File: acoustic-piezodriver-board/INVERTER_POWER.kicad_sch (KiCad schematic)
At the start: 64 parts, among them Q501 AO3400A, Q502 AO3400A, U501 NCE6005AS, U502 LM3478MM, U503 NCE6005AS, U504 LM3478MM

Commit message: [schematic] added adc for temperature measurement, current sense resistors, [layout] component placement, connector placement
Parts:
- added C523, C524: 0.1uF, Capacitor_SMD:C_0402_1005Metric, symbol Device:C_Small
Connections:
- net +BATT: now also C523.1, C524.1
- net GND: now also C523.2, C524.2
- net VDC renamed VDC_P
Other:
- moved on the sheet: R511

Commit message: [piezodriver] Added resistive divider (next) come up with a solution for current sensing (galvanic isolation?)
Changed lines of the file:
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@@
 	(text "DC-DC (SEPIC) VBAT -> 10 V\nCapacitance datasheet recommendations\n- Input capacitance (10-20 uF)\n- Output capacitance (100 uF) "
 		(exclude_from_sim no)
-		(at 334.772 35.306 0)
+		(at 349.758 28.448 0)
 		(effects
 			(font

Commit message: found hal-sensor, replaced with different one for lower voltage signal source impedance, reorganised schematic
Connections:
- net VDC_P: no longer C516.1, C517.1, C518.1, C519.1, D504.1 (K), R512.1
- new net VINV_P: C516.1, C517.1, C518.1, C519.1, D504.1 (K), R512.1
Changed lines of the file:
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@@
 		)
 	)
-	(hierarchical_label "VDC_P"
+	(hierarchical_label "VINV_P"
 		(shape bidirectional)
 		(at 379.73 185.42 0)

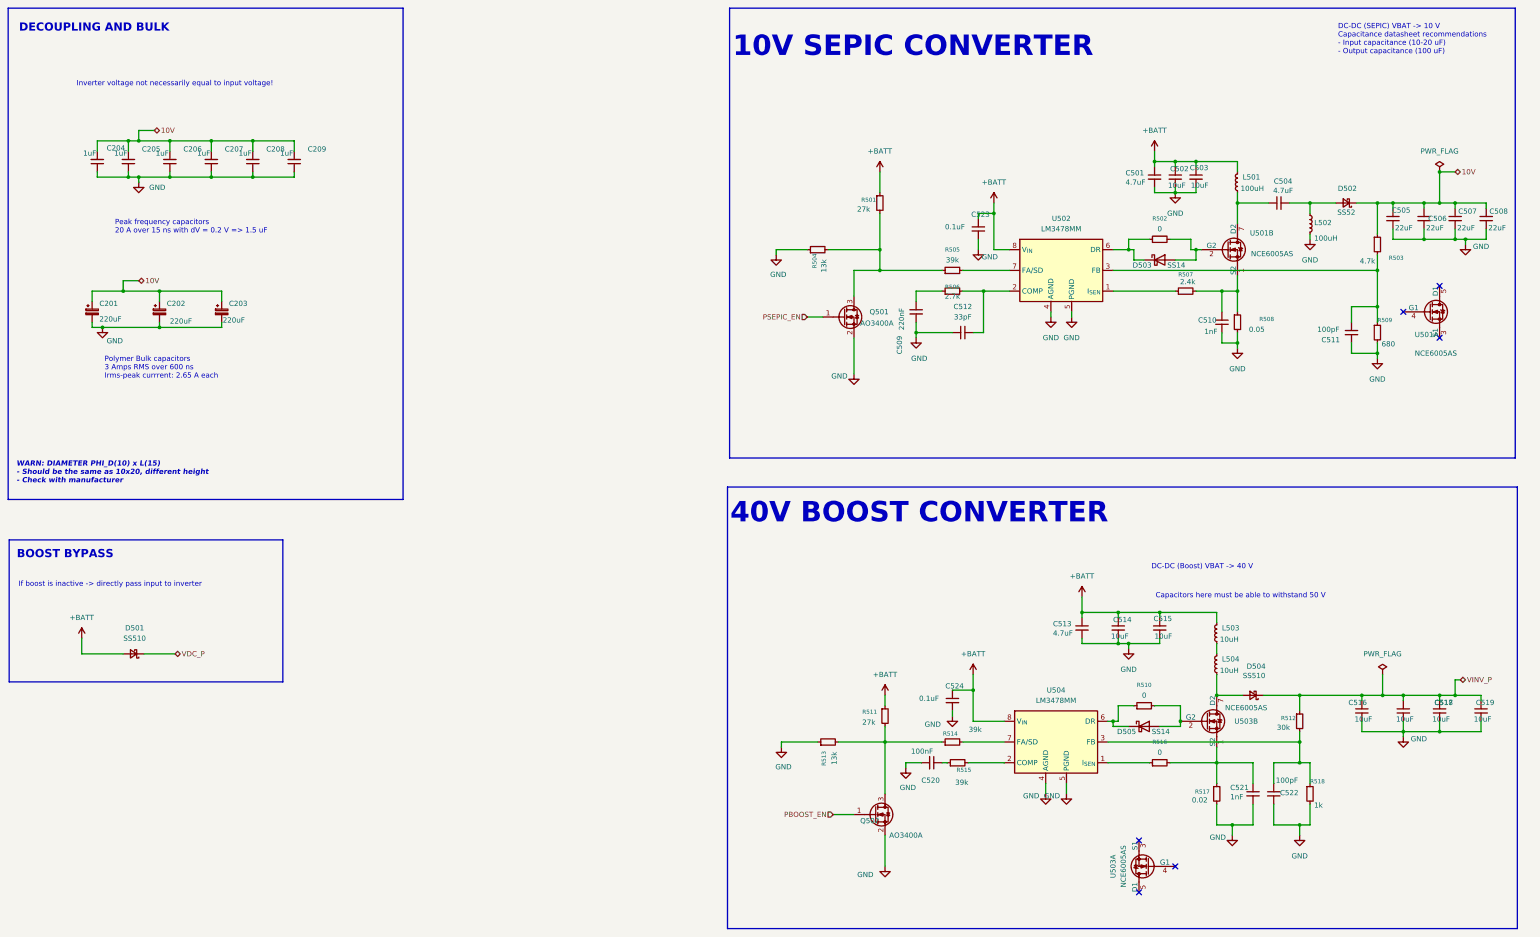
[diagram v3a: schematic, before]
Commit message: added new notes + schematic component hal sensors
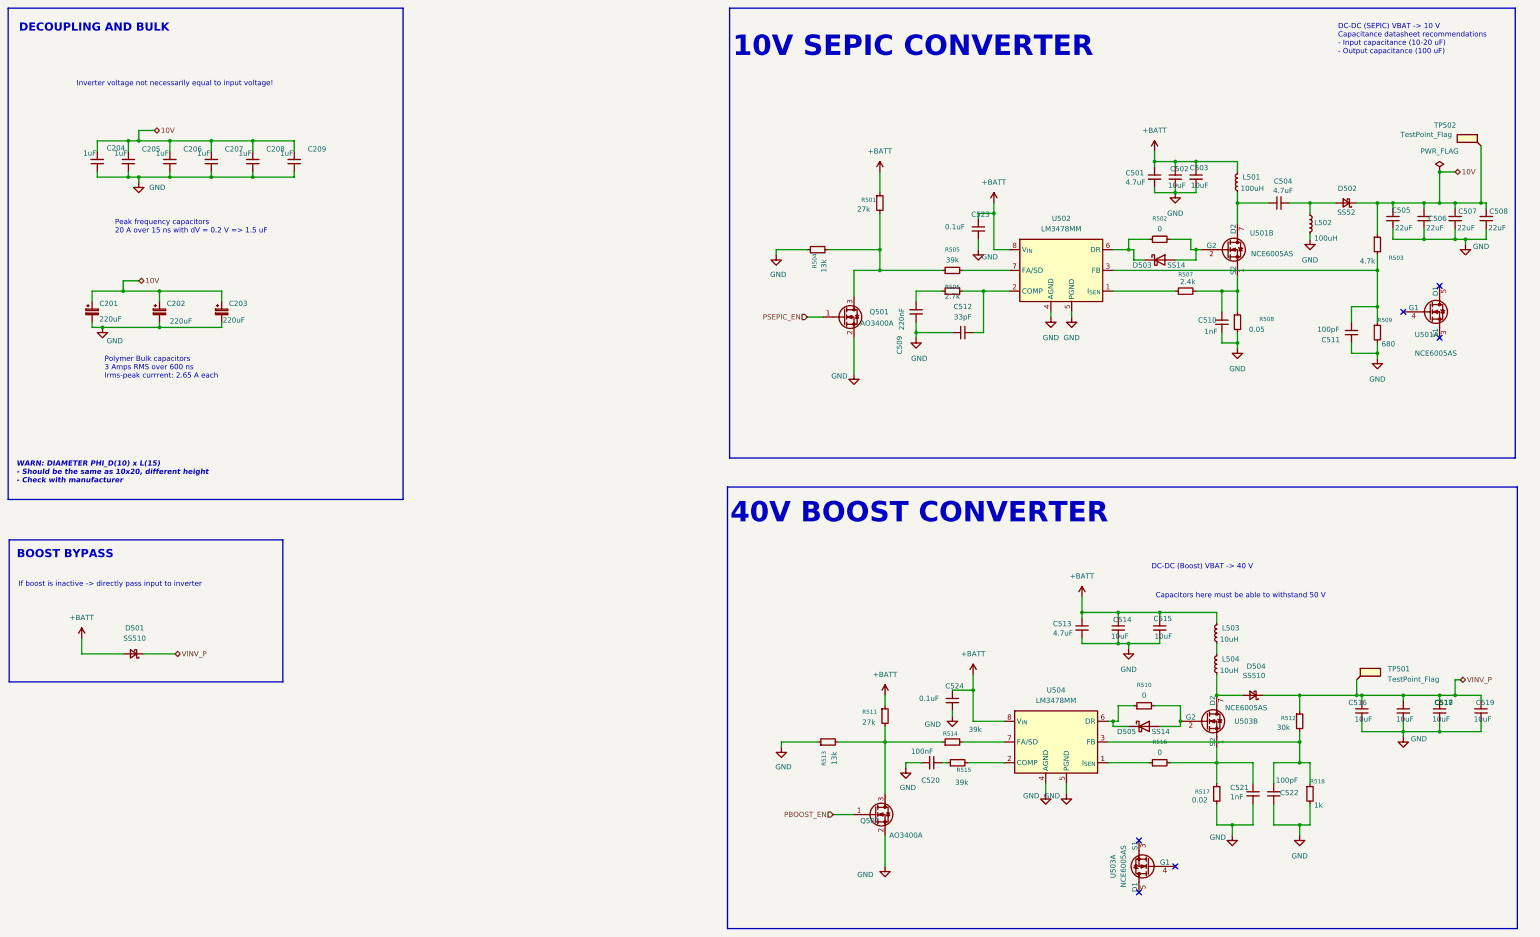
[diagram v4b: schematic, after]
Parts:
- added TP501, TP502: TestPoint_Flag, TestPoint:TestPoint_THTPad_D2.0mm_Drill1.0mm, symbol Connector:TestPoint_Flag
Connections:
- net VDC_P is gone; now on net VINV_P: D501.1 (K)
- net 10V: now also TP502.1
- net VINV_P: now also TP501.1

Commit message: finished schematic, routing
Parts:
- L501, L502: footprint (none) -> iw-inductor:PSPMAA1050H-101M-ANP; LPN C436577 -> C5273830; MPN PSPMAC1045H-101M-ANP -> PSPMAA1050H-101M-ANP
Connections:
- net +BATT: now also L501.1; no longer L501.2
- net at C504.1, U501.7 (D2), U501.8 (D2): now also L501.2; no longer L501.1
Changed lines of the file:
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@@
 	)
 	(symbol
+		(lib_id "Device:L_Small")
+		(at 342.9 73.66 0)
+		(unit 1)
+		(exclude_from_sim no)
+		(in_bom yes)
+		(on_board yes)
+		(dnp no)
+		(fields_autoplaced yes)
+		(property "Reference" "L502"
+			(at 344.17 72.3899 0)
+			(effects
+				(font
+					(size 1.27 1.27)
+				)
+				(justify left)
+			)
+		)
+		(property "Value" "100uH"
+			(at 344.17 74.9299 0)
+			(effects
+				(font
+					(size 1.27 1.27)
+				)
+				(justify left)
+			)
+		)
+		(property "Footprint" "iw-inductor:PSPMAA1050H-101M-ANP"
+			(at 342.9 73.66 0)
+			(effects
+				(font
+					(size 1.27 1.27)
+				)
+				(hide yes)
+			)
+		)
+		(property "Datasheet" "https://jlcpcb.com/api/file/downloadByFileSystemAccessId/8588935627815862272"
+			(at 342.9 73.66 0)
+			(effects
+				(font
+					(size 1.27 1.27)
+				)
+				(hide yes)
+			)
+		)
+		(property "Description" "+-20%, DCR 0.25, Isat_rms=3A"
+			(at 342.9 73.66 0)
+			(effects
+				(font
+					(size 1.27 1.27)
+				)
+				(hide yes)
+			)
+		)
+		(property "LPN" "C5273830"
+			(at 342.9 73.66 0)
+			(effects
+				(font
+					(size 1.27 1.27)
+				)
+				(hide yes)
+			)
+		)
+		(property "MPN" "PSPMAA1050H-101M-ANP "
+			(at 342.9 73.66 0)
+			(effects
+				(font
+					(size 1.27 1.27)
+				)
+				(hide yes)
+			)
+		)
+		(pin "2"
+		)
+		(pin "1"
+		)
+		(instances
+			(project "acoustic-piezodriver-board"
+				(path "/94cb090f-214e-44cc-b8ed-ae50ff29d2bf/0f73f174-3d76-44ea-b4fb-f42a113ccf94/3fdad211-c35f-4919-8f75-d4bdd008edbf"
+					(reference "L502")
+					(unit 1)
+				)
+			)
+		)
+	)
+	(symbol
 		(lib_id "power:GND")
 		(at 283.21 213.36 0)
@@
 	)
 	(symbol
-		(lib_id "Device:L_Small")
-		(at 325.12 63.5 180)
-		(unit 1)
-		(exclude_from_sim no)
-		(in_bom yes)
-		(on_board yes)
-		(dnp no)
-		(property "Reference" "L501"
-			(at 326.39 62.2299 0)
-			(effects
-				(font
-					(size 1.27 1.27)
-				)
-				(justify right)
-			)
-		)
-		(property "Value" "100uH"
-			(at 325.882 65.024 0)
-			(effects
-				(font
-					(size 1.27 1.27)
-				)
-				(justify right)
-			)
-		)
-		(property "Footprint" ""
-			(at 325.12 63.5 0)
-			(effects
-				(font
-					(size 1.27 1.27)
-				)
-				(hide yes)
-			)
-		)
-		(property "Datasheet" "https://jlcpcb.com/api/file/downloadByFileSystemAccessId/8588935627815862272"
-			(at 325.12 63.5 0)
-			(effects
-				(font
-					(size 1.27 1.27)
-				)
-				(hide yes)
-			)
-		)
-		(property "Description" "+-20%, DCR 0.25, Isat_rms=2A"
-			(at 325.12 63.5 0)
-			(effects
-				(font
-					(size 1.27 1.27)
-				)
-				(hide yes)
-			)
-		)
-		(property "LPN" "C436577"
-			(at 325.12 63.5 0)
-			(effects
-				(font
-					(size 1.27 1.27)
-				)
-				(hide yes)
-			)
-		)
-		(property "MPN" "PSPMAC1045H-101M-ANP"
-			(at 325.12 63.5 0)
-			(effects
-				(font
-					(size 1.27 1.27)
-				)
-				(hide yes)
-			)
-		)
-		(pin "2"
-		)
-		(pin "1"
-		)
-		(instances
-			(project "acoustic-piezodriver-board"
-				(path "/94cb090f-214e-44cc-b8ed-ae50ff29d2bf/0f73f174-3d76-44ea-b4fb-f42a113ccf94/3fdad211-c35f-4919-8f75-d4bdd008edbf"
-					(reference "L501")
-					(unit 1)
-				)
-			)
-		)
-	)
-	(symbol
 		(lib_id "Device:D_Schottky_Small")
 		(at 351.79 68.58 180)
@@
 	)
 	(symbol
-		(lib_id "Device:L_Small")
-		(at 342.9 73.66 0)
-		(unit 1)
-		(exclude_from_sim no)
-		(in_bom yes)
-		(on_board yes)
-		(dnp no)
-		(property "Reference" "L502"
-			(at 343.916 73.406 0)
-			(effects
-				(font
-					(size 1.27 1.27)
-				)
-				(justify left)
-			)
-		)
-		(property "Value" "100uH"
-			(at 343.916 77.216 0)
-			(effects
-				(font
-					(size 1.27 1.27)
-				)
-				(justify left)
-			)
-		)
-		(property "Footprint" ""
-			(at 342.9 73.66 0)
-			(effects
-				(font
-					(size 1.27 1.27)
-				)
-				(hide yes)
-			)
-		)
-		(property "Datasheet" "https://jlcpcb.com/api/file/downloadByFileSystemAccessId/8588935627815862272"
-			(at 342.9 73.66 0)
-			(effects
-				(font
-					(size 1.27 1.27)
-				)
-				(hide yes)
-			)
-		)
-		(property "Description" "+-20%, DCR 0.25, Isat_rms=2A"
-			(at 342.9 73.66 0)
-			(effects
-				(font
-					(size 1.27 1.27)
-				)
-				(hide yes)
-			)
-		)
-		(property "LPN" "C436577"
-			(at 342.9 73.66 0)
-			(effects
-				(font
-					(size 1.27 1.27)
-				)
-				(hide yes)
-			)
-		)
-		(property "MPN" "PSPMAC1045H-101M-ANP"
-			(at 342.9 73.66 0)
-			(effects
-				(font
-					(size 1.27 1.27)
-				)
-				(hide yes)
-			)
-		)
-		(pin "2"
-		)
-		(pin "1"
-		)
-		(instances
-			(project "acoustic-piezodriver-board"
-				(path "/94cb090f-214e-44cc-b8ed-ae50ff29d2bf/0f73f174-3d76-44ea-b4fb-f42a113ccf94/3fdad211-c35f-4919-8f75-d4bdd008edbf"
-					(reference "L502")
-					(unit 1)
-				)
-			)
-		)
-	)
-	(symbol
 		(lib_id "power:+BATT")
 		(at 237.49 60.96 0)
@@
 					(unit 1)
 				)
+			)
+		)
+	)
+	(symbol
+		(lib_id "Device:L_Small")
+		(at 325.12 63.5 0)
+		(unit 1)
+		(exclude_from_sim no)
+		(in_bom yes)
+		(on_board yes)
+		(dnp no)
+		(fields_autoplaced yes)
+		(property "Reference" "L501"
+			(at 326.39 62.2299 0)
+			(effects
+				(font
+					(size 1.27 1.27)
+				)
+				(justify left)
+			)
+		)
+		(property "Value" "100uH"
+			(at 326.39 64.7699 0)
+			(effects
+				(font
+					(size 1.27 1.27)
+				)
+				(justify left)
+			)
+		)
+		(property "Footprint" "iw-inductor:PSPMAA1050H-101M-ANP"
+			(at 325.12 63.5 0)
+			(effects
+				(font
+					(size 1.27 1.27)
+				)
+				(hide yes)
+			)
+		)
+		(property "Datasheet" "https://jlcpcb.com/api/file/downloadByFileSystemAccessId/8588935627815862272"
+			(at 325.12 63.5 0)
+			(effects
+				(font
+					(size 1.27 1.27)
+				)
+				(hide yes)
+			)
+		)
+		(property "Description" "+-20%, DCR 0.25, Isat_rms=3A"
+			(at 325.12 63.5 0)
+			(effects
+				(font
+					(size 1.27 1.27)
+				)
+				(hide yes)
+			)
+		)
+		(property "LPN" "C5273830"
+			(at 325.12 63.5 0)
+			(effects
+				(font
+					(size 1.27 1.27)
+				)
+				(hide yes)
+			)
+		)
+		(property "MPN" "PSPMAA1050H-101M-ANP "
+			(at 325.12 63.5 0)
+			(effects
+				(font
+					(size 1.27 1.27)
+				)
+				(hide yes)
+			)
+		)
+		(pin "2"
+		)
+		(pin "1"
+		)
+		(instances
+			(project "acoustic-piezodriver-board"
+				(path "/94cb090f-214e-44cc-b8ed-ae50ff29d2bf/0f73f174-3d76-44ea-b4fb-f42a113ccf94/3fdad211-c35f-4919-8f75-d4bdd008edbf"
+					(reference "L501")
+					(unit 1)
+				)

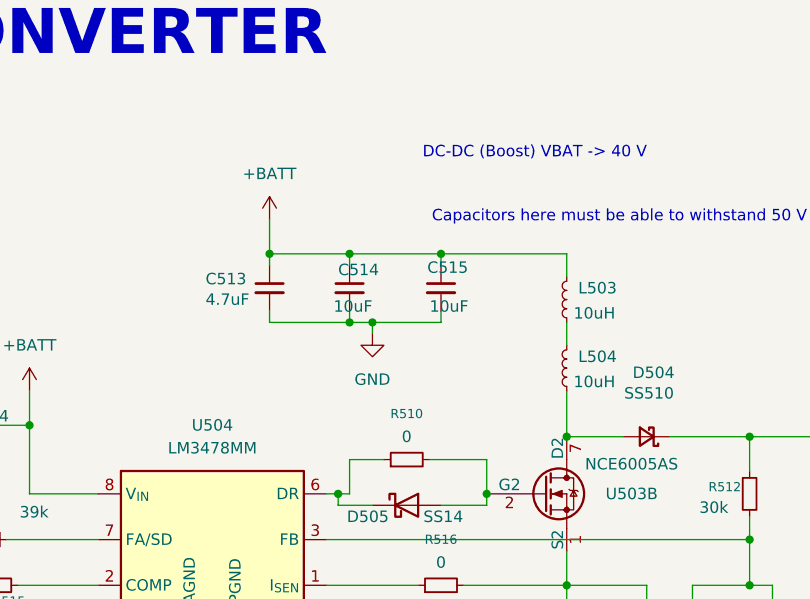
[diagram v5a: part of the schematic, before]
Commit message: replaced dual 10uH inductors with single 22uH higher VDC resistant one, started laying out 40 V boost
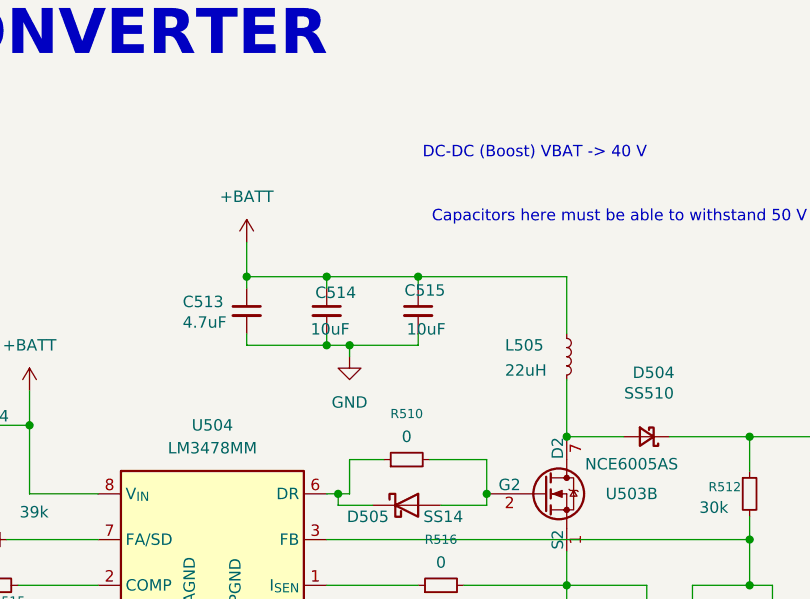
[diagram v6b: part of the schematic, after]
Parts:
- removed L503, L504: 10uH, symbol Device:L_Small
- added L505: 22uH, iw-inductor:PA4343.223NLT, symbol Device:L_Small
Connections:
- net +BATT: now also L505.1
- net at D504.2 (A), U503.7 (D2), U503.8 (D2): now also L505.2
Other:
- moved on the sheet: C513, C514, C515

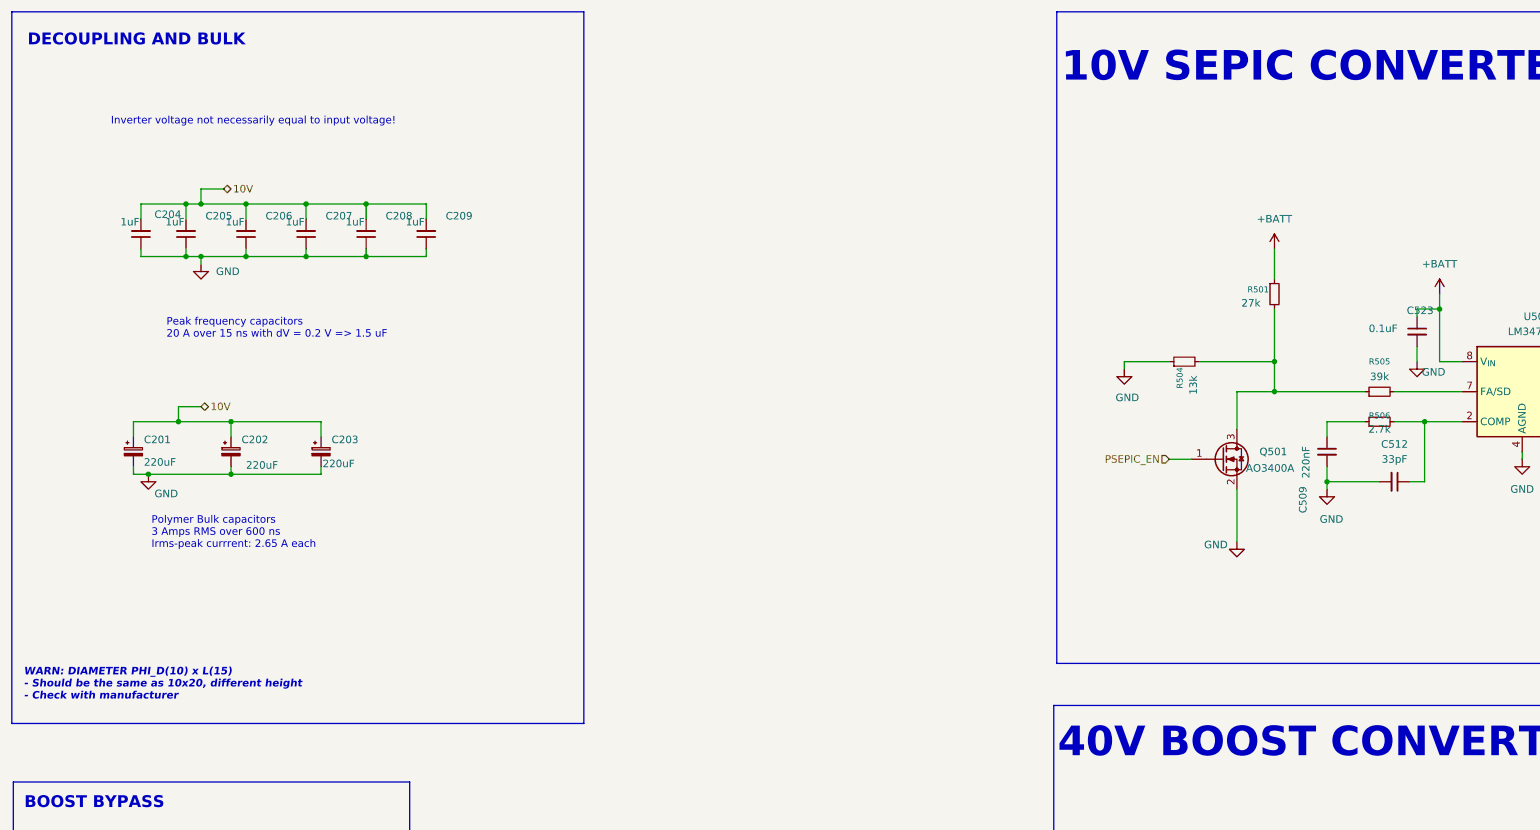
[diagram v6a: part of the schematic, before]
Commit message: placed inverter and 40 V boost (next) place 10 V SEPIC driver
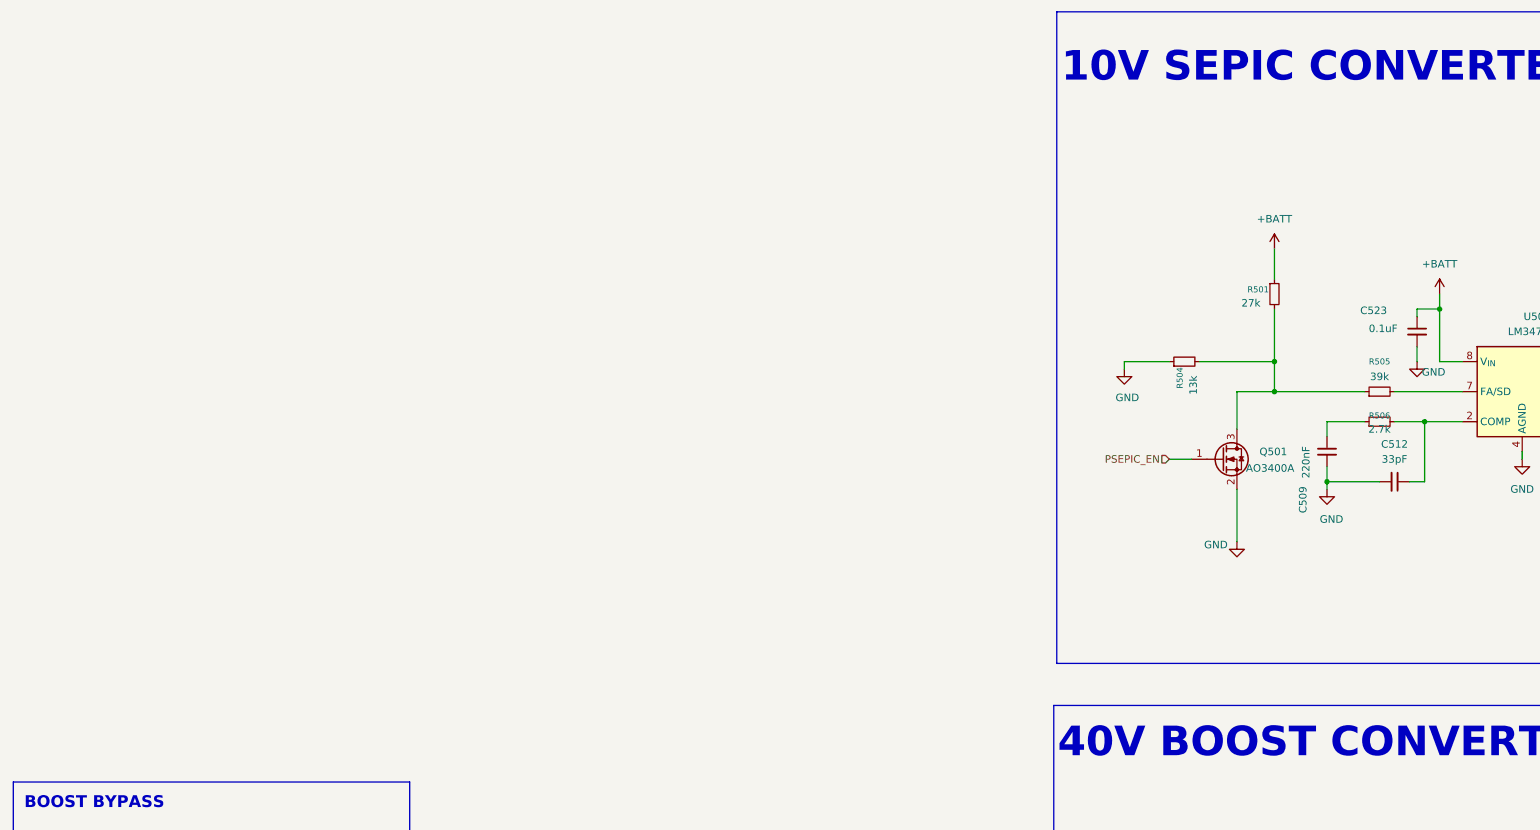
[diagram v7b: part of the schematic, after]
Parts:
- removed C201, C202, C203: 220uF, Capacitor_THT:C_Radial_D10.0mm_H16.0mm_P5.00mm, symbol Device:C_Polarized_Small
- removed C204, C205, C206, C207, C208, C209: 1uF, Capacitor_SMD:C_0805_2012Metric, symbol Device:C_Small
- U502, U504: LPN (none) -> C404045; MPN (none) -> LM3478MMX/NOPB
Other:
- note removed: "DECOUPLING AND BULK"
- note removed: "Inverter voltage not necessarily equal to input voltage!"
- note removed: "Peak frequency capacitors 20 A over 15 ns with dV = 0.2 V => 1.5 uF"
- note removed: "Polymer Bulk capacitors 3 Amps RMS over 600 ns Irms-peak currrent: 2.65 A each"
- note removed: "WARN: DIAMETER PHI_D(10) x L(15) - Should be the same as 10x20, different height - Check with manufacturer"
